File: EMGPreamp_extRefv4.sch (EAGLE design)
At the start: 45 parts

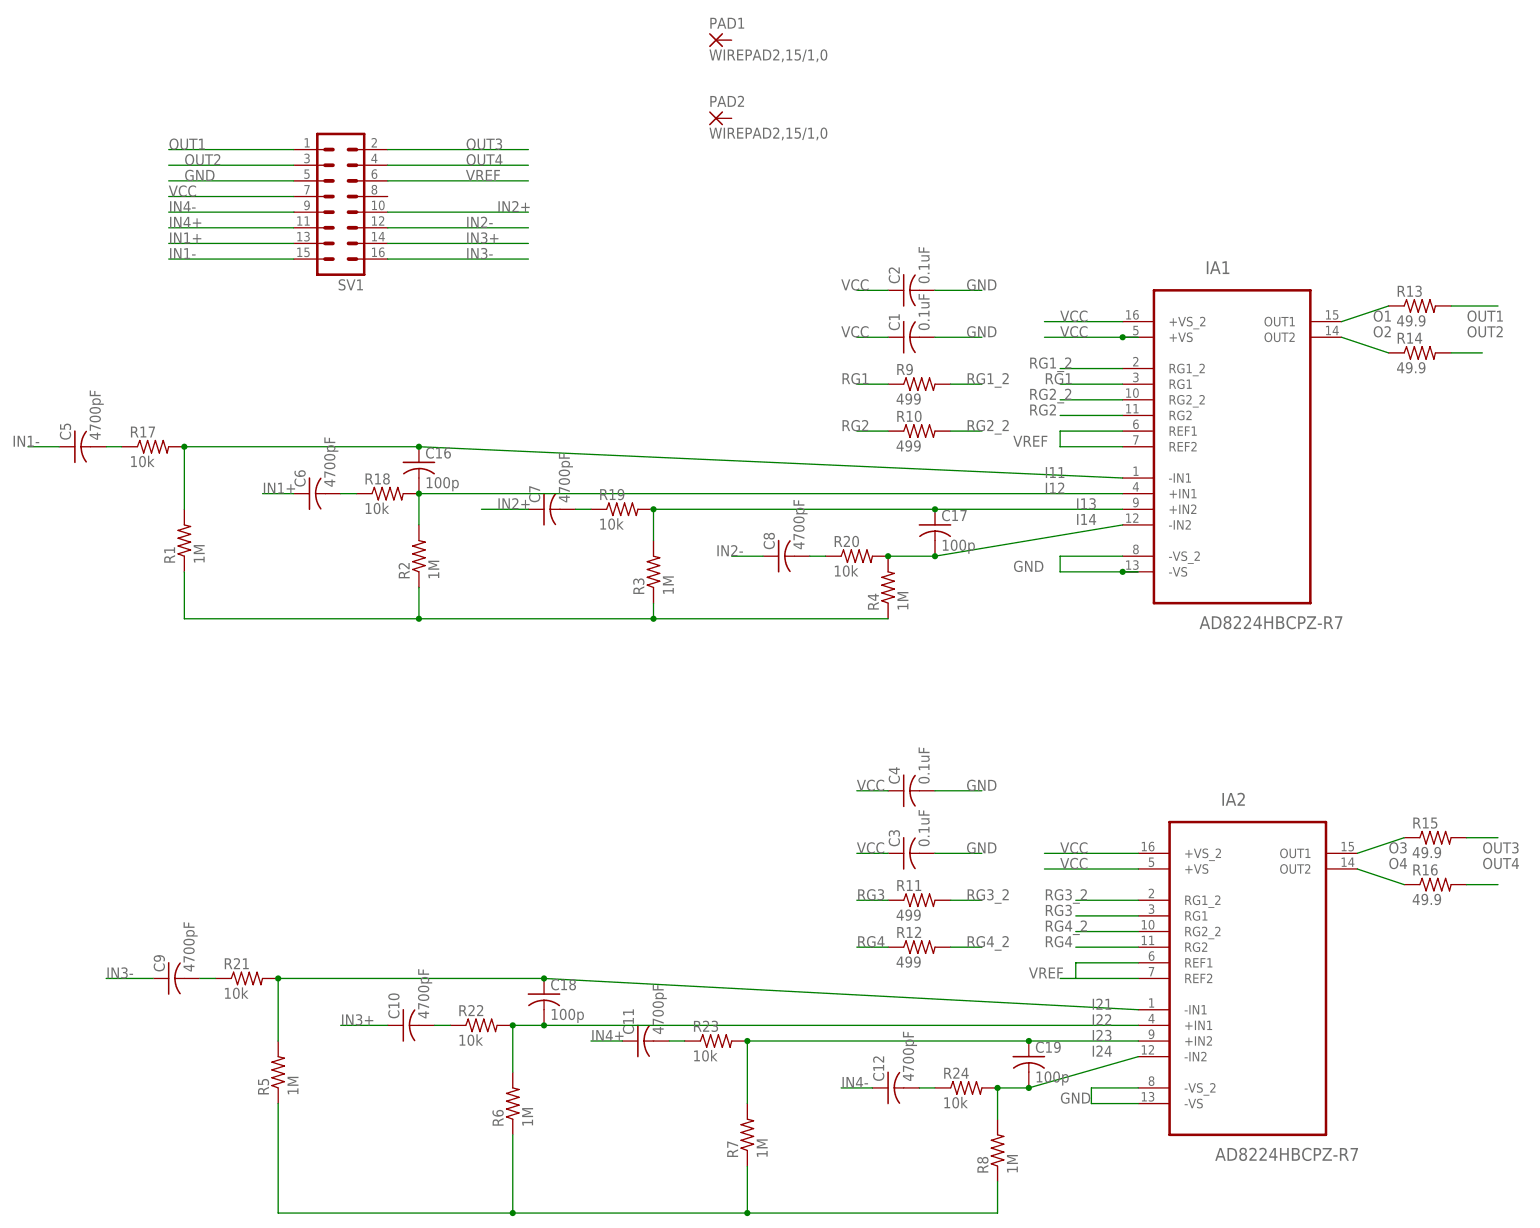
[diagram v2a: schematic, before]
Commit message: updated RF input suppression to include decoupling caps to gnd
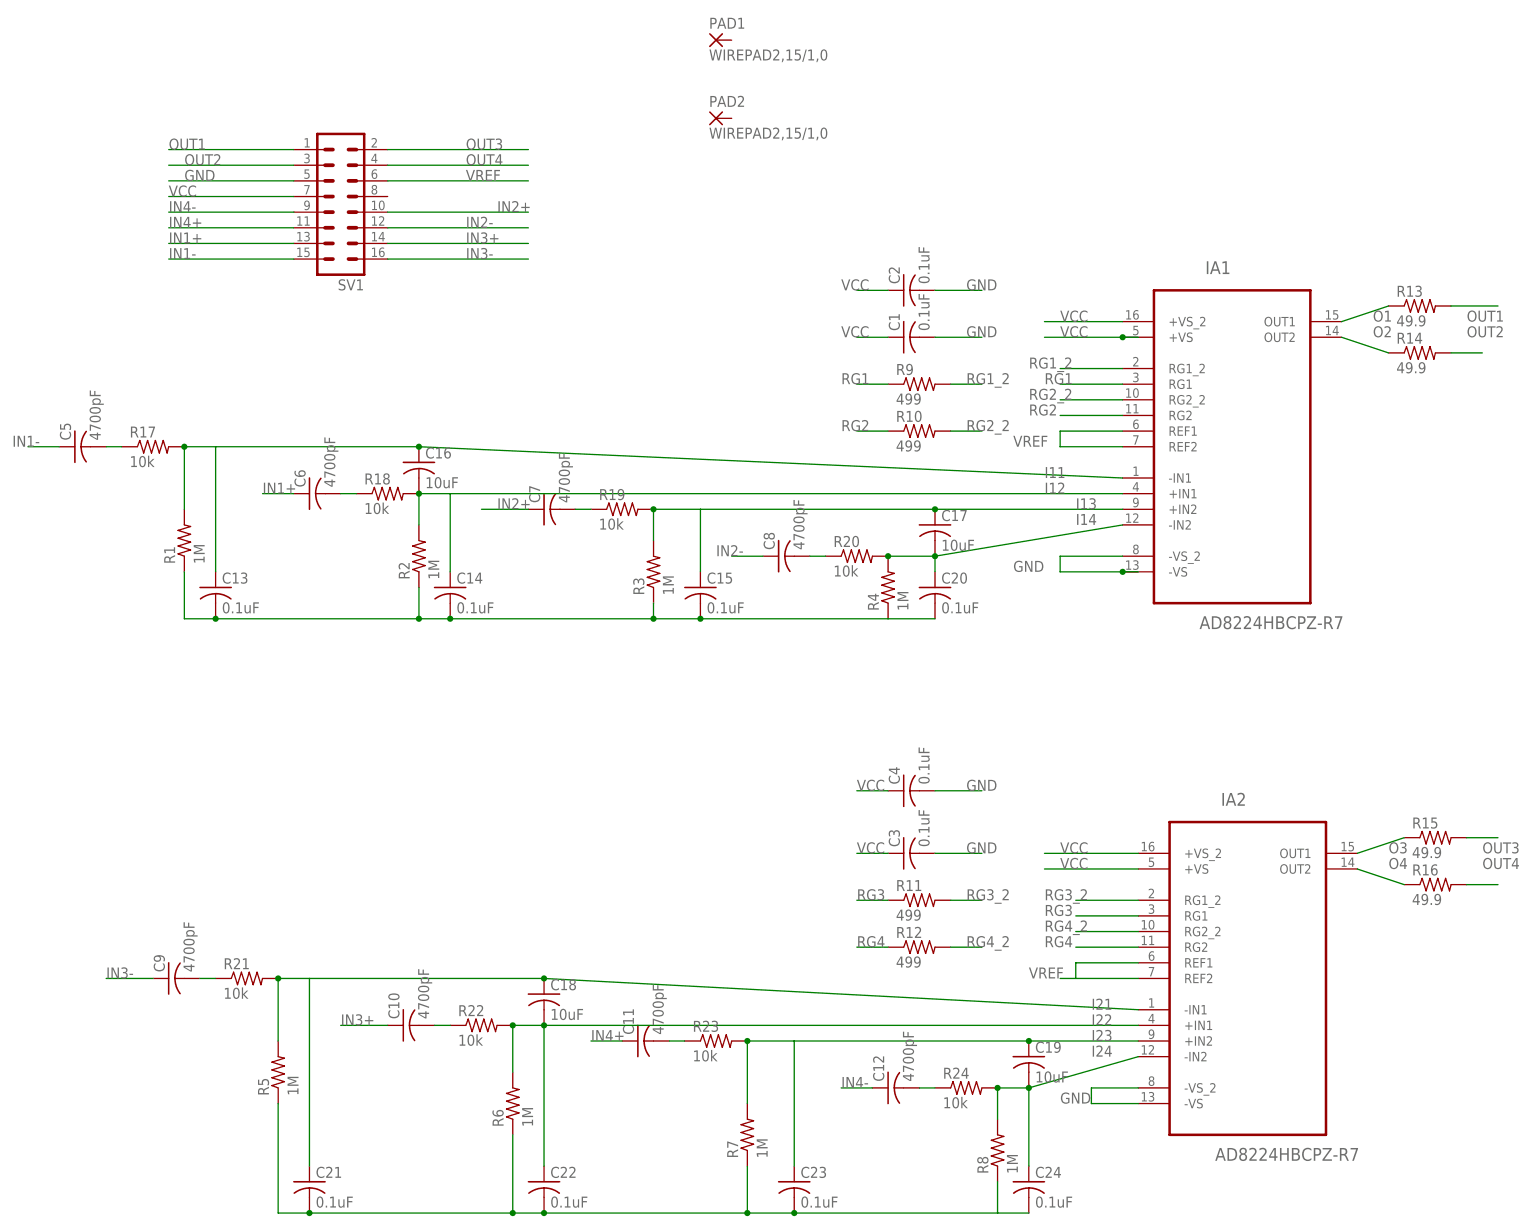
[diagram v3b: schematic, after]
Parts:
- added C13, C14, C15, C20, C21, C22, C23, C24: 0.1uF, rcl:C-USC0805
- C16, C17, C18, C19: value 100p -> 10uF
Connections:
- net GND: now also C13.2, C14.2, C15.2, C20.2, C21.2, C22.2, C23.2, C24.2
- net I11: now also C13.1
- net I12: now also C14.1
- net I13: now also C15.1
- net I14: now also C20.1
- net I21: now also C21.1
- net I22: now also C22.1
- net I23: now also C23.1
- net I24: now also C24.1
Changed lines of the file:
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@@
 <part name="R23" library="resistor" deviceset="R-US_" device="R0805" value="10k"/>
 <part name="R24" library="resistor" deviceset="R-US_" device="R0805" value="10k"/>
-<part name="C16" library="resistor" deviceset="C-US" device="C0805" value="100p"/>
-<part name="C17" library="resistor" deviceset="C-US" device="C0805" value="100p"/>
-<part name="C18" library="resistor" deviceset="C-US" device="C0805" value="100p"/>
-<part name="C19" library="resistor" deviceset="C-US" device="C0805" value="100p"/>
+<part name="C16" library="resistor" deviceset="C-US" device="C0805" value="10uF"/>
+<part name="C17" library="resistor" deviceset="C-US" device="C0805" value="10uF"/>
+<part name="C18" library="resistor" deviceset="C-US" device="C0805" value="10uF"/>
+<part name="C19" library="resistor" deviceset="C-US" device="C0805" value="10uF"/>
+<part name="C13" library="rcl" deviceset="C-US" device="C0805" value="0.1uF"/>
+<part name="C14" library="rcl" deviceset="C-US" device="C0805" value="0.1uF"/>
+<part name="C15" library="rcl" deviceset="C-US" device="C0805" value="0.1uF"/>
+<part name="C20" library="rcl" deviceset="C-US" device="C0805" value="0.1uF"/>
+<part name="C21" library="rcl" deviceset="C-US" device="C0805" value="0.1uF"/>
+<part name="C22" library="rcl" deviceset="C-US" device="C0805" value="0.1uF"/>
+<part name="C23" library="rcl" deviceset="C-US" device="C0805" value="0.1uF"/>
+<part name="C24" library="rcl" deviceset="C-US" device="C0805" value="0.1uF"/>
 </parts>
 <sheets>
@@
 <instance part="C18" gate="G$1" x="-45.72" y="-25.4"/>
 <instance part="C19" gate="G$1" x="33.02" y="-35.56"/>
+<instance part="C13" gate="G$1" x="-99.06" y="40.64"/>
+<instance part="C14" gate="G$1" x="-60.96" y="40.64"/>
+<instance part="C15" gate="G$1" x="-20.32" y="40.64"/>
+<instance part="C20" gate="G$1" x="17.78" y="40.64"/>
+<instance part="C21" gate="G$1" x="-83.82" y="-55.88"/>
+<instance part="C22" gate="G$1" x="-45.72" y="-55.88"/>
+<instance part="C23" gate="G$1" x="-5.08" y="-55.88"/>
+<instance part="C24" gate="G$1" x="33.02" y="-55.88"/>
 </instances>
 <busses>
@@
 <wire x1="-104.14" y1="43.18" x2="-104.14" y2="35.56" width="0.1524" layer="91"/>
 <pinref part="R4" gate="G$1" pin="1"/>
-<wire x1="10.16" y1="35.56" x2="-27.94" y2="35.56" width="0.1524" layer="91"/>
+<wire x1="10.16" y1="35.56" x2="-20.32" y2="35.56" width="0.1524" layer="91"/>
 <pinref part="R2" gate="G$1" pin="1"/>
-<wire x1="-27.94" y1="35.56" x2="-66.04" y2="35.56" width="0.1524" layer="91"/>
-<wire x1="-66.04" y1="35.56" x2="-104.14" y2="35.56" width="0.1524" layer="91"/>
+<wire x1="-20.32" y1="35.56" x2="-27.94" y2="35.56" width="0.1524" layer="91"/>
+<wire x1="-27.94" y1="35.56" x2="-60.96" y2="35.56" width="0.1524" layer="91"/>
+<wire x1="-60.96" y1="35.56" x2="-66.04" y2="35.56" width="0.1524" layer="91"/>
+<wire x1="-66.04" y1="35.56" x2="-99.06" y2="35.56" width="0.1524" layer="91"/>
+<wire x1="-99.06" y1="35.56" x2="-104.14" y2="35.56" width="0.1524" layer="91"/>
 <wire x1="-66.04" y1="40.64" x2="-66.04" y2="35.56" width="0.1524" layer="91"/>
 <junction x="-66.04" y="35.56"/>
@@
 <wire x1="-27.94" y1="38.1" x2="-27.94" y2="35.56" width="0.1524" layer="91"/>
 <junction x="-27.94" y="35.56"/>
+<pinref part="C13" gate="G$1" pin="2"/>
+<junction x="-99.06" y="35.56"/>
+<pinref part="C14" gate="G$1" pin="2"/>
+<junction x="-60.96" y="35.56"/>
+<pinref part="C15" gate="G$1" pin="2"/>
+<junction x="-20.32" y="35.56"/>
+<pinref part="C20" gate="G$1" pin="2"/>
+<wire x1="10.16" y1="35.56" x2="17.78" y2="35.56" width="0.1524" layer="91"/>
 </segment>
 <segment>
@@
 <wire x1="27.94" y1="-55.88" x2="27.94" y2="-60.96" width="0.1524" layer="91"/>
 <pinref part="R5" gate="G$1" pin="1"/>
-<wire x1="27.94" y1="-60.96" x2="-12.7" y2="-60.96" width="0.1524" layer="91"/>
-<wire x1="-12.7" y1="-60.96" x2="-50.8" y2="-60.96" width="0.1524" layer="91"/>
-<wire x1="-50.8" y1="-60.96" x2="-88.9" y2="-60.96" width="0.1524" layer="91"/>
+<wire x1="27.94" y1="-60.96" x2="-5.08" y2="-60.96" width="0.1524" layer="91"/>
+<wire x1="-5.08" y1="-60.96" x2="-12.7" y2="-60.96" width="0.1524" layer="91"/>
+<wire x1="-12.7" y1="-60.96" x2="-45.72" y2="-60.96" width="0.1524" layer="91"/>
+<wire x1="-45.72" y1="-60.96" x2="-50.8" y2="-60.96" width="0.1524" layer="91"/>
+<wire x1="-50.8" y1="-60.96" x2="-83.82" y2="-60.96" width="0.1524" layer="91"/>
+<wire x1="-83.82" y1="-60.96" x2="-88.9" y2="-60.96" width="0.1524" layer="91"/>
 <wire x1="-88.9" y1="-60.96" x2="-88.9" y2="-43.18" width="0.1524" layer="91"/>
 <pinref part="R6" gate="G$1" pin="1"/>
@@
 <wire x1="-12.7" y1="-53.34" x2="-12.7" y2="-60.96" width="0.1524" layer="91"/>
 <junction x="-12.7" y="-60.96"/>
+<pinref part="C21" gate="G$1" pin="2"/>
+<junction x="-83.82" y="-60.96"/>
+<pinref part="C22" gate="G$1" pin="2"/>
+<junction x="-45.72" y="-60.96"/>
+<pinref part="C23" gate="G$1" pin="2"/>
+<junction x="-5.08" y="-60.96"/>
+<pinref part="C24" gate="G$1" pin="2"/>
+<wire x1="33.02" y1="-60.96" x2="27.94" y2="-60.96" width="0.1524" layer="91"/>
 </segment>
 </net>
@@
 <label x="35.56" y="58.42" size="1.778" layer="95"/>
 <pinref part="R1" gate="G$1" pin="2"/>
-<wire x1="-66.04" y1="63.5" x2="-104.14" y2="63.5" width="0.1524" layer="91"/>
+<wire x1="-66.04" y1="63.5" x2="-99.06" y2="63.5" width="0.1524" layer="91"/>
+<wire x1="-99.06" y1="63.5" x2="-104.14" y2="63.5" width="0.1524" layer="91"/>
 <wire x1="-104.14" y1="53.34" x2="-104.14" y2="63.5" width="0.1524" layer="91"/>
 <pinref part="R17" gate="G$1" pin="2"/>
@@
 <pinref part="C16" gate="G$1" pin="1"/>
 <junction x="-66.04" y="63.5"/>
+<pinref part="C13" gate="G$1" pin="1"/>
+<wire x1="-99.06" y1="43.18" x2="-99.06" y2="63.5" width="0.1524" layer="91"/>
 </segment>
 </net>
@@
 <segment>
 <pinref part="IA1" gate="A" pin="+IN1"/>
-<wire x1="48.26" y1="55.88" x2="-66.04" y2="55.88" width="0.1524" layer="91"/>
+<wire x1="48.26" y1="55.88" x2="-60.96" y2="55.88" width="0.1524" layer="91"/>
 <label x="35.56" y="55.88" size="1.778" layer="95"/>
 <pinref part="R2" gate="G$1" pin="2"/>
+<wire x1="-60.96" y1="55.88" x2="-66.04" y2="55.88" width="0.1524" layer="91"/>
 <wire x1="-66.04" y1="50.8" x2="-66.04" y2="55.88" width="0.1524" layer="91"/>
 <pinref part="R18" gate="G$1" pin="2"/>
 <junction x="-66.04" y="55.88"/>
 <pinref part="C16" gate="G$1" pin="2"/>
+<pinref part="C14" gate="G$1" pin="1"/>
+<wire x1="-60.96" y1="43.18" x2="-60.96" y2="55.88" width="0.1524" layer="91"/>
 </segment>
 </net>
@@
 <label x="40.64" y="53.34" size="1.778" layer="95"/>
 <pinref part="R3" gate="G$1" pin="2"/>
-<wire x1="17.78" y1="53.34" x2="-27.94" y2="53.34" width="0.1524" layer="91"/>
+<wire x1="17.78" y1="53.34" x2="-20.32" y2="53.34" width="0.1524" layer="91"/>
+<wire x1="-20.32" y1="53.34" x2="-27.94" y2="53.34" width="0.1524" layer="91"/>
 <wire x1="-27.94" y1="48.26" x2="-27.94" y2="53.34" width="0.1524" layer="91"/>
 <pinref part="R19" gate="G$1" pin="2"/>
@@
 <pinref part="C17" gate="G$1" pin="1"/>
 <junction x="17.78" y="53.34"/>
+<pinref part="C15" gate="G$1" pin="1"/>
+<wire x1="-20.32" y1="43.18" x2="-20.32" y2="53.34" width="0.1524" layer="91"/>
 </segment>
 </net>
@@
 <pinref part="C17" gate="G$1" pin="2"/>
 <junction x="17.78" y="45.72"/>
+<pinref part="C20" gate="G$1" pin="1"/>
+<wire x1="17.78" y1="43.18" x2="17.78" y2="45.72" width="0.1524" layer="91"/>
 </segment>
 </net>
@@
 <label x="43.18" y="-27.94" size="1.778" layer="95"/>
 <pinref part="R5" gate="G$1" pin="2"/>
-<wire x1="-45.72" y1="-22.86" x2="-88.9" y2="-22.86" width="0.1524" layer="91"/>
+<wire x1="-45.72" y1="-22.86" x2="-83.82" y2="-22.86" width="0.1524" layer="91"/>
+<wire x1="-83.82" y1="-22.86" x2="-88.9" y2="-22.86" width="0.1524" layer="91"/>
 <wire x1="-88.9" y1="-33.02" x2="-88.9" y2="-22.86" width="0.1524" layer="91"/>
 <pinref part="R21" gate="G$1" pin="2"/>
@@
 <pinref part="C18" gate="G$1" pin="1"/>
 <junction x="-45.72" y="-22.86"/>
+<pinref part="C21" gate="G$1" pin="1"/>
+<wire x1="-83.82" y1="-53.34" x2="-83.82" y2="-22.86" width="0.1524" layer="91"/>
 </segment>
 </net>
@@
 <pinref part="C18" gate="G$1" pin="2"/>
 <junction x="-45.72" y="-30.48"/>
+<pinref part="C22" gate="G$1" pin="1"/>
+<wire x1="-45.72" y1="-53.34" x2="-45.72" y2="-30.48" width="0.1524" layer="91"/>
 </segment>
 </net>
@@
 <label x="43.18" y="-33.02" size="1.778" layer="95"/>
 <pinref part="R7" gate="G$1" pin="2"/>
-<wire x1="33.02" y1="-33.02" x2="-12.7" y2="-33.02" width="0.1524" layer="91"/>
+<wire x1="33.02" y1="-33.02" x2="-5.08" y2="-33.02" width="0.1524" layer="91"/>
+<wire x1="-5.08" y1="-33.02" x2="-12.7" y2="-33.02" width="0.1524" layer="91"/>
 <wire x1="-12.7" y1="-43.18" x2="-12.7" y2="-33.02" width="0.1524" layer="91"/>
 <pinref part="R23" gate="G$1" pin="2"/>
@@
 <pinref part="C19" gate="G$1" pin="1"/>
 <junction x="33.02" y="-33.02"/>
+<pinref part="C23" gate="G$1" pin="1"/>
+<wire x1="-5.08" y1="-53.34" x2="-5.08" y2="-33.02" width="0.1524" layer="91"/>
 </segment>
 </net>
@@
 <pinref part="C19" gate="G$1" pin="2"/>
 <junction x="33.02" y="-40.64"/>
-</segment>
-</net>
+<pinref part="C24" gate="G$1" pin="1"/>
+<wire x1="33.02" y1="-53.34" x2="33.02" y2="-40.64" width="0.1524" layer="91"/>
+</segment>
+</net>
